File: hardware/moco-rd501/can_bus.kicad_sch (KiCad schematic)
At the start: 12 parts, among them J6 Conn_02x02_Top_Bottom, J7 Conn_02x02_Top_Bottom, U4 MCP25625, Y2 16MHz

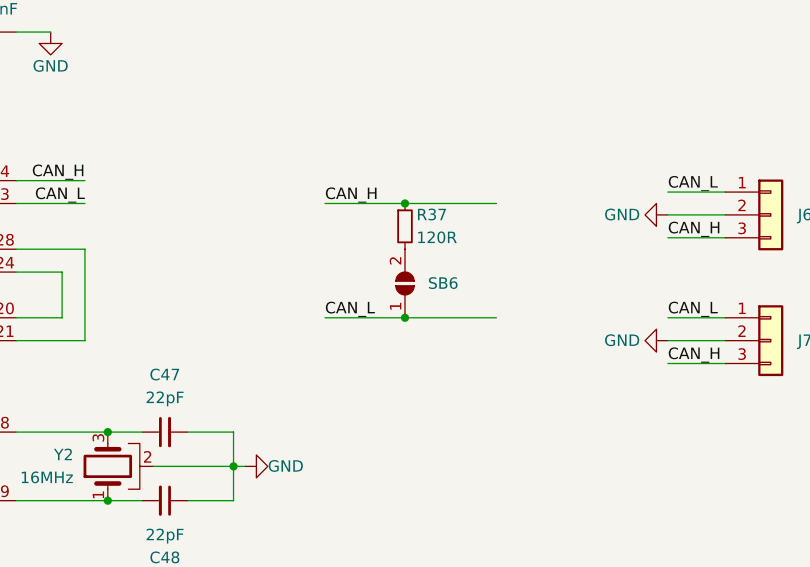
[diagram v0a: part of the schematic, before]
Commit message: Rename "moco-s" to "moco-rd501"
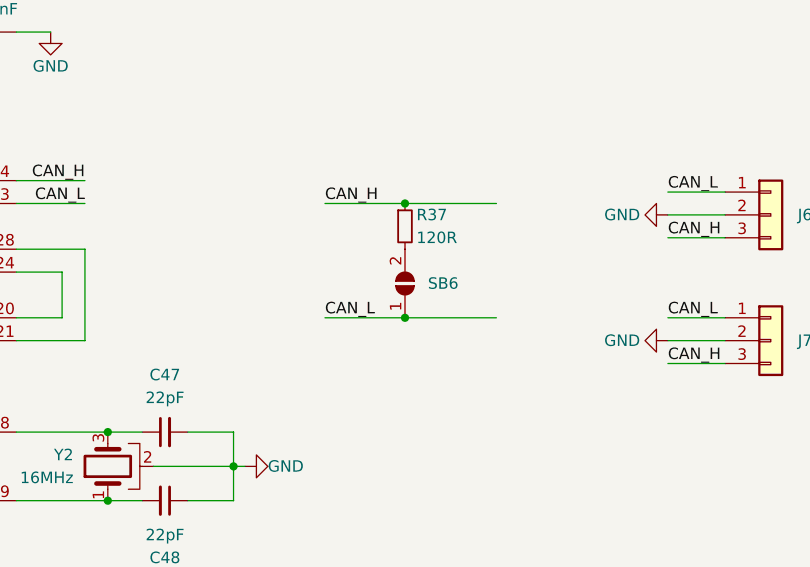
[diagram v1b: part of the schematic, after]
